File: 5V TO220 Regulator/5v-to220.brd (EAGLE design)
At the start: 30.8 x 19 mm, 9 parts

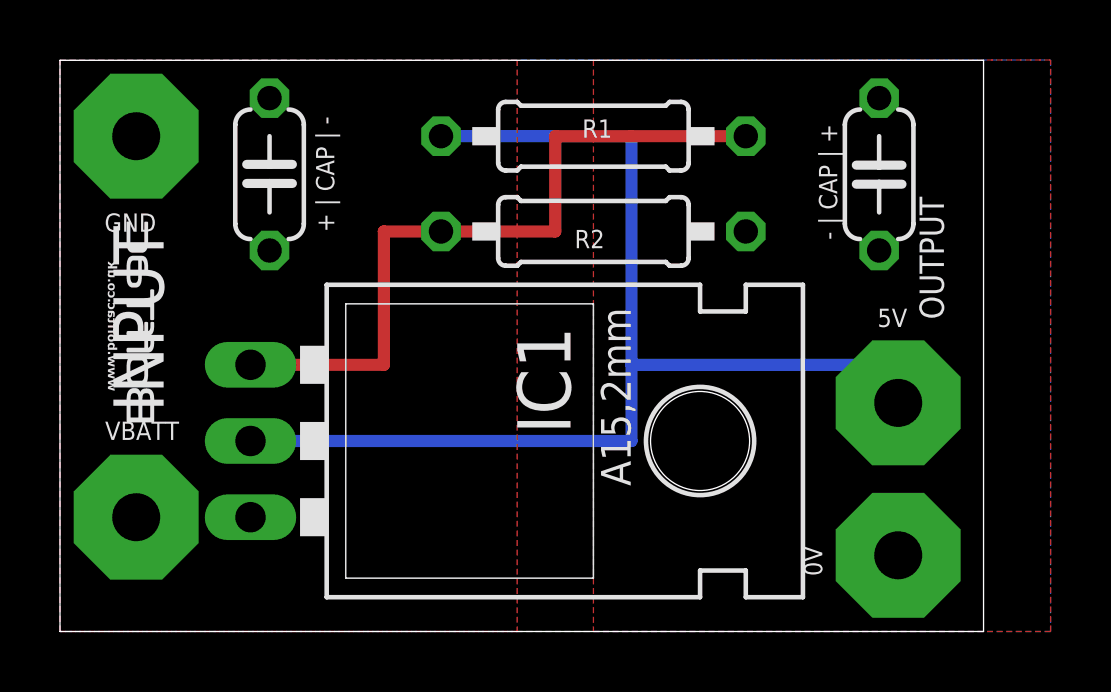
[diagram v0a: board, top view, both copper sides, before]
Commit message: TO220 Reg Update
> Adjusted position of output solder pads to improve cable layouts
> Improved silkscreen labelling
> Rotated caps so +ve and -ve are aligned on all caps
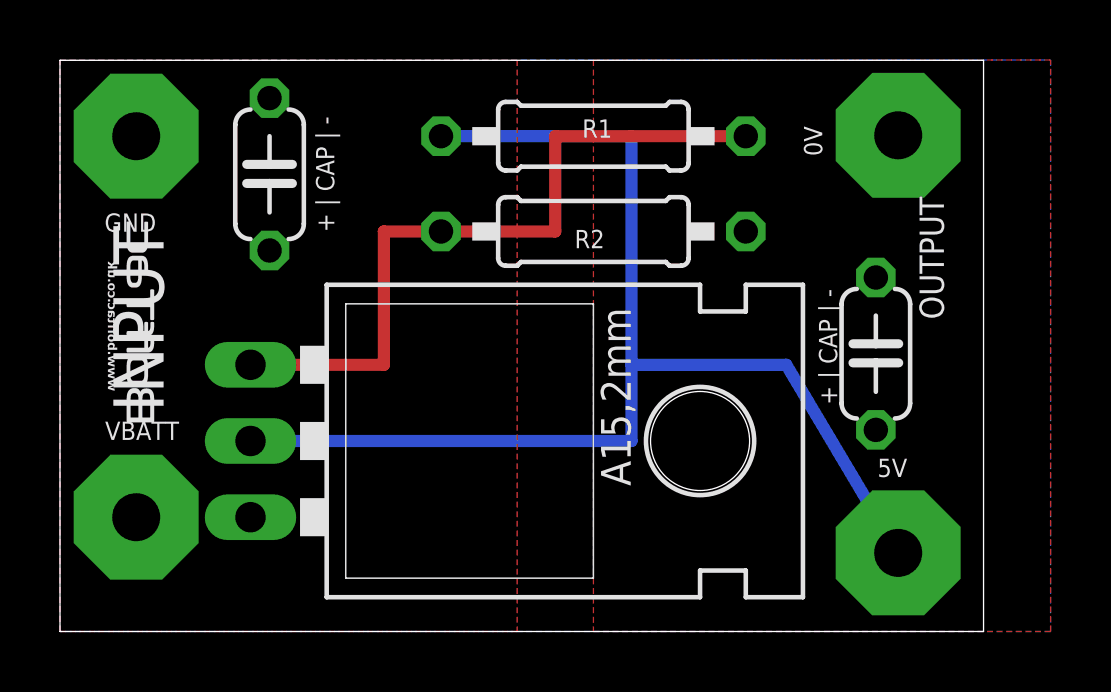
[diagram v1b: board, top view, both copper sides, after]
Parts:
- moved 0V 14.0 mm to (27.9, 16.5)
- moved C2 5.98 mm to (27.2, 9.26), turned to 90 degrees
- moved 5V 5.00 mm to (27.9, 2.62)
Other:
- board text removed: "- | CAP | +"
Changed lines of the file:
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@@
 <setting verticaltext="up"/>
 </settings>
-<grid distance="100" unitdist="mil" unit="mil" style="lines" multiple="1" display="yes" altdistance="10" altunitdist="mil" altunit="mil"/>
+<grid distance="1" unitdist="mm" unit="mm" style="lines" multiple="1" display="yes" altdistance="0.5" altunitdist="mm" altunit="mm"/>
 <layers>
 <layer number="1" name="Top" color="4" fill="1" visible="yes" active="yes"/>
@@
 R2 = 820R</text>
 <text x="9.144" y="15.24" size="0.6096" layer="25" font="vector" ratio="12" rot="R90" align="bottom-center">+ | CAP | -</text>
-<text x="25.908" y="14.986" size="0.6096" layer="25" font="vector" ratio="12" rot="R90" align="bottom-center">- | CAP | +</text>
+<text x="25.908" y="9.486" size="0.6096" layer="25" font="vector" ratio="12" rot="R90" align="bottom-center">+ | CAP | -</text>
 <text x="1.778" y="10.414" size="1.6764" layer="25" font="vector" ratio="12" rot="R270" align="bottom-center">INPUT</text>
 <text x="29.464" y="12.446" size="0.8128" layer="25" font="vector" ratio="12" rot="R90" align="bottom-center">OUTPUT</text>
@@
 </autorouter>
 <elements>
-<element name="0V" library="wirepad" package="4,16O1,6" value="" x="27.94" y="2.54" smashed="yes">
-<attribute name="VALUE" x="27.94" y="2.54" size="0.0254" layer="27"/>
-<attribute name="NAME" x="25.105" y="2.345" size="0.6096" layer="25" rot="R90" align="center"/>
+<element name="0V" library="wirepad" package="4,16O1,6" value="" x="27.94" y="16.54" smashed="yes">
+<attribute name="VALUE" x="27.94" y="16.54" size="0.0254" layer="27"/>
+<attribute name="NAME" x="25.105" y="16.345" size="0.6096" layer="25" rot="R90" align="center"/>
 </element>
-<element name="5V" library="wirepad" package="4,16O1,6" value="" x="27.94" y="7.62" smashed="yes">
-<attribute name="VALUE" x="27.94" y="7.62" size="0.0254" layer="27"/>
-<attribute name="NAME" x="27.745" y="10.455" size="0.6096" layer="25" align="center"/>
+<element name="5V" library="wirepad" package="4,16O1,6" value="" x="27.94" y="2.62" smashed="yes">
+<attribute name="VALUE" x="27.94" y="2.62" size="0.0254" layer="27"/>
+<attribute name="NAME" x="27.745" y="5.455" size="0.6096" layer="25" align="center"/>
 </element>
 <element name="C1" library="resistor" package="C050-024X044" value="" x="6.985" y="15.24" smashed="yes" rot="R90">
 <attribute name="VALUE" x="9.652" y="13.081" size="1.27" layer="27" ratio="10" rot="R90"/>
 </element>
-<element name="C2" library="resistor" package="C050-024X044" value="" x="27.305" y="15.24" smashed="yes" rot="R270">
-<attribute name="VALUE" x="24.638" y="17.399" size="1.27" layer="27" ratio="10" rot="R270"/>
+<element name="C2" library="resistor" package="C050-024X044" value="" x="27.195" y="9.26" smashed="yes" rot="R90">
+<attribute name="VALUE" x="29.862" y="7.101" size="1.27" layer="27" ratio="10" rot="R90"/>
 </element>
 <element name="GND" library="wirepad" package="4,16O1,6" value="" x="2.54" y="16.51" smashed="yes">
@@
 </element>
 <element name="IC1" library="v-reg" package="TO220L1" value="" x="10.16" y="6.35" smashed="yes" rot="R270">
-<attribute name="NAME" x="15.24" y="10.16" size="1.778" layer="25" ratio="10" rot="R270"/>
 <attribute name="VALUE" x="12.7" y="10.287" size="1.778" layer="27" ratio="10" rot="R270"/>
 </element>
@@
 <wire x1="6.35" y1="6.35" x2="19.05" y2="6.35" width="0.4064" layer="16"/>
 <wire x1="19.05" y1="6.35" x2="19.05" y2="8.89" width="0.4064" layer="16"/>
-<wire x1="19.05" y1="8.89" x2="29.21" y2="8.89" width="0.4064" layer="16"/>
-<wire x1="29.21" y1="8.89" x2="27.94" y2="7.62" width="0.4064" layer="16"/>
+<wire x1="19.05" y1="8.89" x2="24.21" y2="8.89" width="0.4064" layer="16"/>
+<wire x1="24.21" y1="8.89" x2="27.94" y2="2.62" width="0.4064" layer="16"/>
 <polygon width="0.4064" layer="1">
 <vertex x="17.78" y="19.05"/>
